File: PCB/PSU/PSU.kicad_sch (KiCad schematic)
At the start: 85 parts, among them J1 Backllight_Connector, J2 PSU_Jack, J3 PSU_Connector_Receptor, Q18 Q, Q22 8C, Q26 G16, Q27 8C, Q29 H15, Q32 K, Q34 6LS, Q5 8C, U12 J412, U13 J421, U5 K2337, U6 7064, U7 5W01, U8 FDS2734, U9 FDS2734

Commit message: Add files via upload
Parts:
- added C1, C16, C28, C46, C5, C59, C7: 150nF, symbol PCM_Elektuur:C
- added C10: 3.6nF, symbol PCM_Elektuur:C
- added C11, C15, C37: 180nF, symbol PCM_Elektuur:C
- added C12: 1.2uF, symbol PCM_Elektuur:C
- added C13, C14, C23, C41, C58: 1.5uF, symbol PCM_Elektuur:C
- added C17, C30, C32, C39, C9: 10nF, symbol PCM_Elektuur:C
- added C2: 4.7uF, symbol PCM_Elektuur:C
- added C21: 12nF, symbol PCM_Elektuur:C
- added C3: 5.2uF, symbol PCM_Elektuur:C
- added C35, C66: 1.2nF, symbol PCM_Elektuur:C
- added C4: 2.5nF, symbol PCM_Elektuur:C
- added C42, C51, C53, C64: 120nF, symbol PCM_Elektuur:C
- added C56, C61: 47uF, symbol PCM_Elektuur:C
- added C57: 15uF, symbol PCM_Elektuur:C
- added C6: 100pF, symbol PCM_Elektuur:C
- added C60: 1nF, symbol PCM_Elektuur:C
- added C62, C65: 100nF, symbol PCM_Elektuur:C
- added C63: 5.1nF, symbol PCM_Elektuur:C
- added C67: 18uF, symbol PCM_Elektuur:C
- added C8: 24nF, symbol PCM_Elektuur:C
- added D2: 5-9, symbol PCM_Elektuur:D
- added D3, R66, R95, R97: DNP, symbol PCM_Elektuur:C
- added D4: 18, symbol Device:D
- added D5: 3^9, symbol Device:D
- added D6, R1, R50, R82, R91: DNP, symbol PCM_Elektuur:R
- added F3: 15, symbol Device:Fuse
- added F4: 10, symbol Device:Fuse
- added L3: 68uH, symbol PCM_Elektuur:L
- added L4: 470uH, symbol PCM_Elektuur:L
- added Q1: R4C, symbol Device:D_Zener_Dual_CommonCathode_AAK_Split
- added Q10: 103 5G, symbol PSU:103_5G
- added Q11, Q14, Q24, Q3, Q6, Q7: 6LS, symbol Simulation_SPICE:PNP
- added Q12: Q, symbol Device:D_Schottky_Dual_CommonCathode_AAK_Split
- added Q13, Q15, Q33, Q37, Q4: 8LR, symbol Simulation_SPICE:NPN
- added Q16, Q17, Q19: M2P, symbol Device:D_Zener_Dual_CommonAnode_KAK
- added Q2: K, symbol Device:D_Dual_Series_KAC_Parallel
- added Q20, Q28, Q31: W6, symbol Device:D_Dual_CommonCathode_AKA
- added Q21, Q23, Q30, Q35: 8C, symbol Simulation_SPICE:NPN
- added Q25: 8LB, symbol Simulation_SPICE:NPN
- added Q36: 3P4J, symbol PCM_Elektuur:Th
- added Q8: 303 5H, symbol PSU:103_5G
- added Q9: KD 3.E, Package_TO_SOT_SMD:SOT-89-3, symbol Regulator_Linear:L78L05_SOT89
- added R10, R2, R21, R31, R74, R90: 470k, symbol PCM_Elektuur:R
- added R103, R11, R117, R13, R17, R19, R20, R30, R33, R35, R4, R61, R85: 10k, symbol PCM_Elektuur:R
- added R106, R27, R39, R41, R58, R60: 4.7k, symbol PCM_Elektuur:R
- added R107: 2k, symbol PCM_Elektuur:R
- added R109, R81: 200k, symbol PCM_Elektuur:R
- added R111: 33, symbol PCM_Elektuur:R
- added R112, R113, R18, R9: 20k, symbol PCM_Elektuur:R
- added R114, R15, R22, R54, R59, R72, R77, R84, R92: 100k, symbol PCM_Elektuur:R
- added R115: 11k, symbol PCM_Elektuur:R
- added R116: 15k, symbol PCM_Elektuur:R
- added R118, R48: 100, symbol PCM_Elektuur:R
- added R12: 2.2k, symbol PCM_Elektuur:R
- added R14: 12k, symbol PCM_Elektuur:R
- added R16: 130k, symbol PCM_Elektuur:R
- added R23, R25, R34: 0.1, symbol PCM_Elektuur:R
- added R24: 220, symbol PCM_Elektuur:R
- added R26: 103 (RT1), symbol PCM_Elektuur:R
- added R28: 0, symbol PCM_Elektuur:R
- added R29: 103 (RT2), symbol PCM_Elektuur:R
- added R3, R36, R65, R71, R75, R76, R93: 1k, symbol PCM_Elektuur:R
- added R37: 120, symbol PCM_Elektuur:R
- added R38, R6: 470, symbol PCM_Elektuur:R
- added R42, R47, R51, R70, R73, R79, R87, R94: 47k, symbol PCM_Elektuur:R
- added R53, R78: 300k, symbol PCM_Elektuur:R
- added R68: 74k, symbol PCM_Elektuur:R
- added R88, R89: 1M, symbol PCM_Elektuur:R
- added R96: 1.8k, symbol PCM_Elektuur:R
- added SW1: PSU-SW1, symbol Switch:SW_Push
- added U1: D9D, Package_TO_SOT_SMD:SOT-23-5, symbol Power_Management:BD48ExxG
- added U10: ~, symbol PSU:9742
- added U11, UU11: 7W14, symbol 74xGxx:74LVC3G14
- added U2: ~, symbol PSU:TA
- added U3: ~, symbol PSU:6.5_5F
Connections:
- net D18_2_3_PC110: now also J1.1 (Pin_1)
- net D28_1_PC110: now also C11.1 (+), C57.1 (+), C6.2 (-), Q10.4, R16.2 (-)
- net D2_3_PC110: now also Q23.1 (C)
- net F65_ENAVEE_PC110: now also R15.1 (+)
- net GND: now also R69.2 (-), C1.1 (+), C11.2 (-), C12.1 (+), C13.2 (-), C14.2 (-), C15.2 (-), C16.2 (-), C17.1 (+), C23.1 (+), C28.1 (+), C3.1 (+), C30.1 (+), C37.1 (+), C39.2 (-), C41.1 (+), C42.2 (-), C46.2 (-), C51.1 (+), C56.2 (-), C57.2 (-), C58.2 (-), C59.2 (-), C60.1 (+), C61.2 (-), C62.2 (-), C64.2 (-), C65.2 (-), C67.1 (+), C8.2 (-), C9.1 (+), D3.1 (+), D6.1 (+), Q10.2 (GND), Q12.1 (A), Q13.3 (E), Q19.2 (A), Q21.3 (E), Q23.3 (E), Q25.3 (E), Q33.3 (E), Q35.3 (E), Q36.1 (K-), Q37.3 (E), Q4.3 (E), Q8.2 (GND), Q9.2 (GND), R106.2 (-), R113.2 (-), R114.2 (-), R115.2 (-), R116.2 (-), R18.2 (-), R27.2 (-), R33.2 (-), R35.2 (-), R39.2 (-), R53.1 (+), R58.1 (+), R60.2 (-), R72.1 (+), R77.2 (-), R88.1 (+), R9.1 (+), R91.1 (+), R94.2 (-), R95.2 (-), R96.2 (-), U1.3 (GND), U10.8 (GND), U11.4 (GND), U2.2 (GND), U3.3 (GND); no longer R69.1 (+)
- net J5_33_PC110: now also C39.1 (+), R92.1 (+), R93.2 (-)
- net JRC_VCC: now also Q3.3 (E), R3.1 (+)
- net M38_P20_PC110: now also Q28.1 (A), Q37.2 (B)
- net M38_P21_PC110: now also Q28.3 (A)
- net M38_P52_PC110: now also R2.1 (+)
- net M38_P53_PC110: now also Q31.1 (A)
- net M38_P61_PC110: now also R42.1 (+)
- net M38_P64_PC110: now also U6.7, R54.2 (-), R66.2 (-)
- net M38_VREF_PC110: now also C1.2 (-), Q1.3 (K), Q14.3 (E), R6.1 (+)
- net PNET4_PC110: now also C53.2 (-), D2.2 (A+), Q11.3 (E), R22.2 (-)
- net PNET5_PC110: now also C28.2 (-), C56.1 (+), C61.1 (+), C62.1 (+), Q15.1 (C), Q2.3 (common), R118.1 (+), R17.2 (-), R20.2 (-), R23.1 (+), R25.1 (+), R26.1 (+), R29.2 (-), R34.1 (+), R84.2 (-), U11.8 (VCC), U2.5 (VCC)
- net PWR_IN_10v5: now also Q32.2 (A), C30.2 (-), D4.2 (A), Q24.3 (E), Q36.2 (A+), R75.2 (-), R95.1 (+)
- net Q49_1_PC110: now also D5.2 (A), R82.2 (-)
- net R284_2_PC110: now also C13.1 (+), C14.1 (+), F3.2, F4.2
- net R412_1_PC110: now also J1.2 (Pin_2)
- net R73_2_PC110: now also R79.2 (-)
- net U21_131_PC110: now also R10.2 (-)
- net U54_1D_PC110: now also R36.2 (-); no longer C31.1 (+), Q26.2 (G)
- net U54_VCC_PC110: now also C3.2 (-), Q3.2 (B), Q9.1 (OUT), SW1.2
- net at F5.2, L1.1 (+), Q34.3 (E): now also C37.2 (-), R89.2 (-), R91.2 (-)
- net at R52.1 (+), U6.12 (+): now also R69.1 (+), Q19.1 (K); no longer R69.2 (-)
- net at C27.1 (+), R55.1 (+), U7.1: now also Q16.1 (K)
- net at C29.1 (+), J2.2, R98.1 (+): now also R97.2 (-)
- net at C29.2 (-), F1.1, R99.1 (+): now also R97.1 (+)
- net at Q22.1 (C): now also Q35.1 (C), R73.2 (-)
- net at Q22.2 (B), Q5.2 (B), R5.2 (-): now also Q4.2 (B)
- net at U13.4 (G): now also U3.1, U3.4
- net at L1.2 (-), U13.5 (D), U13.6 (D)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: now also D6.2 (-)
- net at L5.1 (+), U4.15 (CS5): now also R23.2 (-), R25.2 (-), R34.2 (-)
- net at C18.1 (+), L5.2 (-), U4.17 (LX5)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: now also Q12.3 (K)
- net at JX.2 (Pin_2), R49.1 (+), R63.2 (-)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: now also Q19.3 (K)
- net at U7.3 (+): now also C46.1 (+), R103.1 (+), R109.1 (+), R113.1 (+)
- net at Q32.3 (common): now also R41.1 (+), R61.2 (-), U3.6
- net at C18.2 (-), U4.18 (BST5): now also Q17.1 (K)
- net at R5.1 (+): now also Q3.1 (C)
- net at C55.2 (-), U4.22 (VL): now also Q17.2 (A), R48.1 (+)
- net at U7.5 (+): now also R106.1 (+), R107.1 (+), R112.1 (+)
- net at U7.6 (-): now also C21.1 (+), R42.2 (-)
- net at U7.7: now also C21.2 (-), Q16.3 (K)
- net at Q34.2 (B): now also R90.1 (+)
- net at U6.5 (+): now also R77.1 (+), R78.1 (+)
- net at U6.6 (-): now also R53.2 (-), R54.1 (+), R66.1 (+)
- net at U4.12 (SHDN#), U4.13 (ON5), U4.3 (ON3)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: now also C23.2 (-), R48.2 (-)
- net at C19.2 (-), U4.25 (BST3): now also Q17.3 (K)
- new net: R93.1 (+), R94.1 (+), SW1.1
- new net: Q24.1 (C), R74.1 (+)
- new net: Q24.2 (B), R78.2 (-)
- new net: C31.1 (+), Q26.2 (G), R36.1 (+)
- new net: C41.2 (-), U10.15 (SCP)
- new net: C63.1 (+), C66.1 (+), U10.5 (FB1)
- new net: C63.2 (-), R117.1 (+), R13.2 (-), R33.1 (+), U10.4 (INV1)
- new net: R71.1 (+), R75.1 (+)
- new net: Q20.3 (A), R27.1 (+), R29.1 (+)
- new net: C17.2 (-), C32.2 (-), C67.2 (-), Q8.4, R81.2 (-)
- new net: C9.2 (-), Q7.1 (C), R15.2 (-), U10.7 (OUT1)
- new net: C8.1 (+), Q6.1 (C), R10.1 (+)
- new net: C60.2 (-), R65.1 (+), U10.1 (CT)
- new net: R50.2 (-), R65.2 (-), U2.3
- new net: C32.1 (+), Q7.3 (E), R115.1 (+), R79.1 (+), R81.1 (+), U10.3 (NON1)
- new net: C6.1 (+), Q6.3 (E), R116.1 (+), R16.1 (+), U10.14 (NON2)
- new net: Q16.2 (A), R51.1 (+), R60.1 (+)
- new net: Q21.1 (C), R59.1 (+)
- new net: Q28.2 (K), Q31.3 (A), R47.2 (-), R59.2 (-)
- new net: R28.1 (+), R31.2 (-), U1.1 (VOUT)
- new net: R21.2 (-), R28.2 (-)
- new net: C2.1 (+), R4.1 (+)
- new net: R1.2 (-), R11.1 (+), R35.1 (+), R4.2 (-), U10.13 (INV2)
- new net: D4.1 (K), R76.1 (+)
- new net: C42.1 (+), Q36.3 (G), R76.2 (-), R96.1 (+)
- new net: C5.2 (-), R18.1 (+), R19.1 (+), U10.11 (DT2)
- new net: C5.1 (+), C58.1 (+), C59.1 (+), C7.2 (-), Q6.2 (B), Q7.2 (B), R11.2 (-), R13.1 (+), R14.1 (+), R19.2 (-), U10.16 (VREF)
- new net: Q21.2 (B), R68.2 (-)
- new net: Q30.3 (E), R50.1 (+), U2.4
- new net: C4.1 (+), R24.2 (-)
- new net: C4.2 (-), R12.2 (-), U11.2
- new net: Q20.1 (A), R26.2 (-), R58.2 (-)
- new net: Q14.2 (B), R68.1 (+)
- new net: L4.1 (+), Q8.3, Q8.5
- new net: C65.1 (+), F4.1, L4.2 (-)
- new net: C7.1 (+), R14.2 (-), R9.2 (-), U10.6 (DT1)
- new net: Q10.1, R37.1 (+), R38.1 (+)
- new net: C10.1 (+), R38.2 (-), U11.5, UU11.7
- new net: Q23.2 (B), R71.2 (-), R72.2 (-), R73.1 (+)
- new net: R88.2 (-), R89.1 (+)
- new net: Q2.1 (K), R3.2 (-)
- new net: Q4.1 (C), R2.2 (-)
- new net: Q1.1 (A), Q14.1 (C), R103.2 (-), R109.2 (-), R112.2 (-)
- new net: R20.1 (+), U11.6
- new net: Q13.1 (C), R30.1 (+)
- new net: D2.1 (K-), Q11.2 (B), R30.2 (-)
- new net: C16.1 (+), R21.1 (+), R22.1 (+), U1.2 (VDD)
- new net: Q15.2 (B), R47.1 (+)
- new net: Q15.3 (E), R51.2 (-)
- new net: R17.1 (+), U10.10 (OUT2), U11.3, UU11.1
- new net: Q31.2 (K), R70.1 (+), R87.2 (-)
- new net: Q25.2 (B), R70.2 (-)
- new net: Q33.1 (C), R90.2 (-)
- new net: Q33.2 (B), R87.1 (+)
- new net: D5.1 (K), Q20.2 (K), R82.1 (+)
- new net: C64.1 (+), R118.2 (-), U10.9 (VCC)
- new net: C2.2 (-), R1.1 (+), U10.12 (FB2)
- new net: Q13.2 (B), R31.1 (+)
- new net: C12.2 (-), D3.2 (-), Q11.1 (C), Q9.3 (IN)
- new net: Q25.1 (C), R74.2 (-)
- new net: Q2.2 (A), R6.2 (-)
- new net: C66.2 (-), R117.2 (-)
- new net: C35.2 (-), Q30.1 (C), R85.2 (-)
- new net: Q30.2 (B), R84.1 (+)
- new net: Q35.2 (B), R92.2 (-)
- new net: C15.1 (+), F3.1, L3.1 (+)
- new net: C51.2 (-), R111.1 (+)
- new net: C53.1 (+), R111.2 (-)
- new net: C10.2 (-), R37.2 (-)
- new net: L3.2 (-), Q10.3, Q10.5
- new net: Q37.1 (C), R107.2 (-)
- new net: C35.1 (+), R61.1 (+), R85.1 (+), U3.2, U3.5
- new net: Q8.1, R12.1 (+), R24.1 (+)
- new net: R39.1 (+), R41.2 (-)
- new net: R114.1 (+), U10.2 (RT)
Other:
- moved on the sheet: C18, C19, C20, C22, C24, C25, C26, C27, C29, C31, C33, C34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

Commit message: Add files via upload
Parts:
- added unit 2 of Q1
- added unit 2 of Q12
- renumbered JX to JX1, UU11 to U11
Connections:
- net GND: now also Q12.2 (A)
- net M38_VREF_PC110: now also Q1.3 (K)
- net Q43_2_PC110: now also C17.2 (-), C32.2 (-), C67.2 (-), Q8.4, R81.2 (-)
- net at Q16.2 (A), R51.1 (+), R60.1 (+): now also U2.1
- net at C18.1 (+), L5.2 (-), Q12.3 (K)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: now also Q12.3 (K)
- no-connect marks 2 -> 3

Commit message: Add files via upload
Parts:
- removed D1: 8-2, symbol Device:D
- removed Q11, Q14, Q24: 6LS, symbol Simulation_SPICE:PNP
- removed Q12: Q, symbol Device:D_Schottky_Dual_CommonCathode_AAK_Split
- removed Q13, Q15, Q33, Q37: 8LR, symbol Simulation_SPICE:NPN
- removed Q22, Q23, Q27, Q30, Q35, Q5: 8C, symbol Simulation_SPICE:NPN
- removed Q25: 8LB, symbol Simulation_SPICE:NPN
- removed Q26: G16, Package_TO_SOT_THT:TO-92_Inline, symbol Transistor_FET:2N7000
- removed Q29: H15, Package_TO_SOT_THT:TO-92L_Inline, symbol Transistor_FET:TP0610L
- removed Q32: K, symbol Device:D_Dual_Series_KAC_Parallel
- added D1: 8-2, symbol Device:D_Zener
- added Q11, Q14: 6LS, symbol PCM_Transistor_BJT_AKL:Q_PNP_Generic_BEC
- added Q12: Q, symbol Device:D_Zener_Dual_CommonAnode_KAK
- added Q13, Q15, Q25, Q33, Q37: 8LR, symbol PCM_Transistor_BJT_AKL:Q_NPN_Generic_BEC
- added Q22, Q5: 8C, symbol PCM_Transistor_BJT_AKL:Q_NPN_Generic_CEB
- added Q23, Q27, Q30, Q35: 8C, symbol PCM_Transistor_BJT_AKL:Q_NPN_Generic_BEC
- added Q24: 6LS, symbol PCM_Transistor_BJT_AKL:Q_PNP_Generic_CEB
- added Q26: G16, PCM_Package_TO_SOT_SMD_AKL:SOT-23, symbol PCM_Transistor_MOSFET_AKL:2N7002AQ
- added Q29: H15, Package_TO_SOT_SMD:SOT-23, symbol Transistor_FET:AO3401A
- added Q32: K, symbol Device:D_Dual_Series_ACK_Parallel
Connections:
- net D2_3_PC110: now also Q23.3 (C)
- net GND: now also C34.2 (-), C56.1 (+), C58.1 (+), C62.1 (+), Q1.1 (A), R105.2 (-), R116.1 (+), R27.1 (+), Q12.1 (K), Q12.3 (K), Q13.2 (E), Q22.2 (E), Q23.2 (E), Q25.2 (E), Q26.2 (S), Q27.2 (E), Q33.2 (E), Q35.2 (E), Q37.2 (E), Q5.2 (E); no longer C34.1 (+), C56.2 (-), C58.2 (-), C62.2 (-), R105.1 (+), R116.2 (-), R27.2 (-)
- net J5_6_PC110: now also D1.1 (K), Q32.1 (A)
- net M38_P20_PC110: now also Q37.1 (B)
- net M38_P60_PC110: now also C25.1 (+), R62.1 (+); no longer C25.2 (-), R62.2 (-)
- net M38_P61_PC110: now also C52.1 (+), R101.1 (+); no longer C52.2 (-), R101.2 (-)
- net M38_P64_PC110: now also R54.1 (+), R66.1 (+); no longer R54.2 (-), R66.2 (-)
- net M38_VREF_PC110: now also Q14.2 (E)
- net PNET4_PC110: now also D2.1 (K-), Q11.2 (E), Q29.2 (S); no longer D2.2 (A+)
- net PNET5_PC110: now also C56.2 (-), C62.2 (-), Q15.3 (C); no longer C56.1 (+), C62.1 (+)
- net PWR_IN_10v5: now also D4.1 (K), Q24.2 (E), Q32.3 (K); no longer D4.2 (A)
- net U54_VCC_PC110: now also SW1.1; no longer SW1.2
- net at R93.1 (+), R94.1 (+): now also SW1.2; no longer SW1.1
- net at R74.1 (+): now also Q24.1 (C)
- net at R78.2 (-): now also Q24.3 (B)
- net at F5.1, JX1.1 (Pin_1): no longer R52.2 (-)
- net at C31.1 (+), R36.1 (+): now also Q26.1 (G)
- net at C27.1 (+), R55.1 (+): now also R67.1 (+), U7.2 (-); no longer Q16.1 (K), U7.1
- net at C27.2 (-), R55.2 (-): now also Q16.1 (K), U7.1; no longer R67.1 (+), U7.2 (-)
- net at Q20.3 (A), R29.1 (+): now also R27.2 (-); no longer R27.1 (+)
- net at R46.1 (+): now also Q26.3 (D), Q29.1 (G)
- net at R73.2 (-): now also Q22.1 (C), Q35.3 (C)
- net at Q4.2 (B), R5.2 (-): now also Q22.3 (B), Q5.3 (B)
- net at C6.1 (+), Q6.3 (E), R16.1 (+)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: now also R116.2 (-); no longer R116.1 (+)
- net at JX1.2 (Pin_2), R49.1 (+), R63.2 (-)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: now also R52.2 (-); no longer Q19.3 (K)
- net at C18.1 (+), L5.2 (-), U4.17 (LX5)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: now also Q12.2 (A)
- net at R63.1 (+), U6.9 (-): now also C25.2 (-), Q19.3 (K), R62.2 (-); no longer C25.1 (+), R62.1 (+)
- net at R76.1 (+): now also D4.2 (A); no longer D4.1 (K)
- net at C5.1 (+), C59.1 (+), C7.2 (-)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: now also C58.2 (-); no longer C58.1 (+)
- net at R50.1 (+), U2.4: now also Q30.2 (E)
- net at R64.2 (-), U6.13 (-): now also C52.2 (-), R101.2 (-); no longer C52.1 (+), R101.1 (+)
- net at R68.1 (+): now also Q14.1 (B)
- net at R41.1 (+), R61.2 (-), U3.6: now also Q32.2 (common)
- net at R53.2 (-), U6.6 (-): now also R54.2 (-), R66.2 (-); no longer R54.1 (+), R66.1 (+)
- net at R71.2 (-), R72.2 (-), R73.1 (+): now also Q23.1 (B)
- net at C36.2 (-), R83.2 (-), R86.1 (+)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: now also Q29.3 (D)
- net at C33.2 (-): now also C34.1 (+), R80.1 (+), Q27.1 (B); no longer R86.2 (-)
- net at R103.2 (-), R109.2 (-), R112.2 (-): now also Q14.3 (C); no longer Q1.1 (A)
- net at R30.1 (+): now also Q13.3 (C)
- net at R30.2 (-): now also D2.2 (A+), Q11.1 (B); no longer D2.1 (K-)
- net at R47.1 (+): now also Q15.1 (B)
- net at R51.2 (-): now also Q15.2 (E)
- net at R70.2 (-): now also Q25.1 (B)
- net at R90.2 (-): now also Q33.3 (C)
- net at R87.1 (+): now also Q33.1 (B)
- net at C43.1 (+), R102.1 (+), U6.3 (+): now also R105.1 (+); no longer R105.2 (-)
- net at R31.1 (+): now also Q13.1 (B)
- net at C12.2 (-), D3.2 (-), Q9.3 (IN): now also Q11.3 (C)
- net at R74.2 (-): now also Q25.3 (C)
- net at R85.2 (-): now also C35.1 (+), R61.1 (+), U3.2, U3.5; no longer C35.2 (-)
- net at R84.1 (+): now also Q30.1 (B)
- net at R92.2 (-): now also Q35.1 (B)
- net at R107.2 (-): now also Q37.3 (C)
- new net: C33.1 (+), Q27.3 (C), R86.2 (-)
- new net: D1.2 (A), Q5.1 (C)
- new net: C35.2 (-), Q30.3 (C), R85.1 (+)
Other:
- moved on the sheet: C1, C25, C27, C33, C34, C52, C58, C62, Q1A, R101, R105, R116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

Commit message: Add files via upload
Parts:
- removed Q4: 8LR, symbol Simulation_SPICE:NPN
- added Q4: 8LR, symbol PCM_Transistor_BJT_AKL:Q_NPN_Generic_CEB
- C1, C10, C11, C15, C16, C17, C18, C19, C21, C22, C24, C25, C26, C27, C28, C29, C30, C31, C32, C33, C35, C36, C37, C39, C4, C40, C42, C43, C44, C46, C47, C48, C49, C5, C51, C52, C53, C59, C6, C60, C62, C63, C64, C65, C66, C7, C8, C9: footprint (none) -> Capacitor_SMD:C_0603_1608Metric; Indicator + -> (none); Rating V -> (none)
- C12, C13, C14, C3: footprint (none) -> Capacitor_SMD:C_1206_3216Metric; Indicator + -> (none); Rating V -> (none)
- C2: value 4.7uF -> 4.7nF; footprint (none) -> Capacitor_SMD:C_0603_1608Metric; Indicator + -> (none); Rating V -> (none)
- C20: value 1.2nF -> 100pF; footprint (none) -> Capacitor_SMD:C_0603_1608Metric; Indicator + -> (none); Rating V -> (none)
- C23, C34, C38, C41, C55, C58: footprint (none) -> Capacitor_SMD:C_0805_2012Metric; Indicator + -> (none); Rating V -> (none)
- C45: value 33uF -> 33uF 20V; footprint (none) -> Capacitor_THT:C_Disc_D3.0mm_W1.6mm_P2.50mm; Indicator + -> (none); Rating V -> (none)
- C50: value 56uF -> 56uF 25V EC; footprint (none) -> Capacitor_THT:EC; Indicator + -> (none); Rating V -> (none)
- C54, C61: value 47uF -> 47uF 6.3v; footprint (none) -> Capacitor_THT:C_Radial_D6.3mm_H11.0mm_P2.50mm; Indicator + -> (none); Rating V -> (none)
- C56: value 47uF -> 47uF 6.3V; footprint (none) -> Capacitor_THT:C_Radial_D6.3mm_H11.0mm_P2.50mm; Indicator + -> (none); Rating V -> (none)
- C57: value 15uF -> 15uF 16V; footprint (none) -> Capacitor_THT:C_Radial_D6.3mm_H11.0mm_P2.50mm; Indicator + -> (none); Rating V -> (none)
- C67: value 18uF -> 18uF 50V; footprint (none) -> Capacitor_THT:C_Radial_D6.3mm_H11.0mm_P2.50mm; Indicator + -> (none); Rating V -> (none)
- D1, D4, D5: footprint (none) -> Diode_SMD:D_0603_1608Metric
- D2: footprint (none) -> Diode_SMD:D_0603_1608Metric; Rating V/A -> (none)
- D3: footprint (none) -> Diode_SMD:D_1206_3216Metric; Indicator + -> (none); Rating V -> (none); now not fitted
- D6: footprint (none) -> Diode_SMD:D_1206_3216Metric; Indicator + -> (none); Rating W -> (none); now not fitted
- D7, D8: footprint (none) -> Diode_SMD:D_1206_3216Metric; Rating V/A -> (none)
- F1, F2, F5: footprint (none) -> Fuse:Fuse_2010_5025Metric
- F3: footprint (none) -> Fuse:Fuse_1206_3216Metric
- F4: footprint (none) -> Fuse:Fuse_1210_3225Metric
- J1: footprint (none) -> Connector_JST:Backllight_Connector
- J2: footprint (none) -> PSU:PSU_Jack
- J3: footprint (none) -> PSU:PSU_Connector_Receptor
- L1: footprint (none) -> Inductor_THT:L_Radial_D7.5mm_P5.00mm_Fastron_07P; Indicator ● -> (none); Rating A -> (none)
- L2, L5: footprint (none) -> Inductor_THT:L_Radial_D10.0mm_P5.00mm_Fastron_07M; Indicator ● -> (none); Rating A -> (none)
- L3, L4: footprint (none) -> Inductor_SMD:L_Coilcraft_LPS5030; Indicator ● -> (none); Rating A -> (none)
- Q1, Q12, Q16, Q17, Q18, Q19, Q2, Q20, Q28, Q31, Q32: footprint (none) -> PC110:3D
- Q10, Q8: footprint (none) -> Package_TO_SOT_SMD:SOT-powerT
- Q11, Q13, Q14, Q15, Q21, Q22, Q23, Q24, Q27, Q3, Q30, Q33, Q34, Q35, Q37, Q5, Q6, Q7: footprint (none) -> Package_TO_SOT_SMD:SOT-416
- Q25: value 8LR -> 8LB; footprint (none) -> Package_TO_SOT_SMD:SOT-416
- Q26: footprint PCM_Package_TO_SOT_SMD_AKL:SOT-23 -> Package_TO_SOT_SMD:SOT-23-PC110
- Q29: footprint Package_TO_SOT_SMD:SOT-23 -> Package_TO_SOT_SMD:SOT-23-PC110
- Q36: footprint (none) -> Package_TO_SOT_SMD:TO-252-2; Rating V/A -> (none)
- R1: footprint (none) -> Resistor_SMD:R_0603_1608Metric; Indicator + -> (none); Rating W -> (none); now not fitted
- R10, R100, R101, R102, R103, R104, R105, R106, R107, R108, R109, R11, R110, R111, R112, R113, R116, R117, R118, R12, R13, R14, R15, R16, R17, R18, R19, R2, R20, R21, R22, R24, R27, R28, R3, R30, R31, R33, R35, R36, R37, R38, R39, R4, R41, R42, R43, R44, R45, R46, R47, R48, R49, R5, R50, R52, R53, R54, R55, R56, R57, R58, R59, R6, R60, R61, R62, R63, R64, R65, R67, R69, R71, R73, R74, R75, R76, R77, R78, R79, R80, R81, R82, R83, R84, R85, R86, R88, R89, R9, R90, R92, R93, R94, R96: footprint (none) -> Resistor_SMD:R_0603_1608Metric; Indicator + -> (none); Rating W -> (none)
- R114: value 100k -> 10k; footprint (none) -> Resistor_SMD:R_0603_1608Metric; Indicator + -> (none); Rating W -> (none)
- R115: value 11k -> 11K; footprint (none) -> Resistor_SMD:R_0603_1608Metric; Indicator + -> (none); Rating W -> (none)
- R23, R25, R26, R29, R32, R34, R40, R91, R98, R99: footprint (none) -> Resistor_SMD:R_1206_3216Metric; Indicator + -> (none); Rating W -> (none)
- R51: value 47k -> 4.7k; footprint (none) -> Resistor_SMD:R_0603_1608Metric; Indicator + -> (none); Rating W -> (none)
- R66: footprint (none) -> Resistor_SMD:R_0603_1608Metric; Indicator + -> (none); Rating V -> (none); now not fitted
- R68: value 74k -> 47k; footprint (none) -> Resistor_SMD:R_0603_1608Metric; Indicator + -> (none); Rating W -> (none)
- R7, R8: footprint (none) -> Resistor_SMD:R_1210_3225Metric; Indicator + -> (none); Rating W -> (none)
- R70, R87: value 47k -> 470k; footprint (none) -> Resistor_SMD:R_0603_1608Metric; Indicator + -> (none); Rating W -> (none)
- R72: value 100k -> 1k; footprint (none) -> Resistor_SMD:R_0603_1608Metric; Indicator + -> (none); Rating W -> (none)
- R95, R97: footprint (none) -> Resistor_SMD:R_1206_3216Metric; Indicator + -> (none); Rating V -> (none); now not fitted
- SW1: footprint (none) -> PSU:PSU-SW1
- U10: value ~ -> 9742; footprint (none) -> Package_SO:SSOP-16_4.4x5.2mm_P0.65mm
- U11, U7: footprint (none) -> PSU:SSOP-8-PSU
- U12: value J412 -> J421; footprint Package_SO:SOIC-8_3.9x4.9mm_P1.27mm -> Package_SO:SOP-8_3.9x4.9mm_P1.27mm
- U13, U5: footprint Package_SO:SOIC-8_3.9x4.9mm_P1.27mm -> Package_SO:SOP-8_3.9x4.9mm_P1.27mm
- U2: value ~ -> TA; footprint (none) -> Package_TO_SOT_SMD:SOT-23-5
- U3: value ~ -> 6.5 5F; footprint (none) -> Package_TO_SOT_SMD:SOT-23-6_Handsoldering
- U4: value ~ -> MAX786CAI; footprint (none) -> Package_SO:TSSOP-28_6.1x9.7mm_P0.65mm
- U6: footprint (none) -> Package_SO:TSSOP-14_4.4x5mm_P0.65mm
- U8, U9: value FDS2734 -> 2556; footprint Package_SO:SOIC-8_3.9x4.9mm_P1.27mm -> Package_SO:SOP-8_3.9x4.9mm_P1.27mm
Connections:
- net GND: now also Q4.2 (E)
- net at R2.2 (-): now also Q4.1 (C)
- net at Q22.3 (B), Q5.3 (B), R5.2 (-): now also Q4.3 (B)
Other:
- moved on the sheet: C31

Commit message: Add files via upload
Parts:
- Q4: footprint (none) -> Package_TO_SOT_SMD:SOT-416
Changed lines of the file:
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@@
 			)
 		)
-		(property "Footprint" ""
+		(property "Footprint" "Package_TO_SOT_SMD:SOT-416"
 			(at 246.38 256.54 0)
 			(effects
@@
 			)
 		)
-		(property "Description" "NPN transistor, generic symbol, Alternate KiCAD Library"
+		(property "Description" ""
 			(at 251.46 259.08 0)
 			(effects

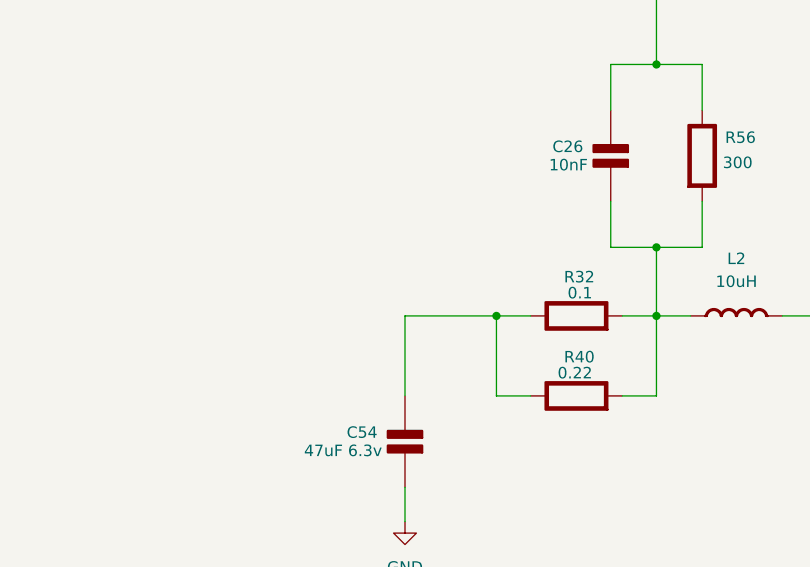
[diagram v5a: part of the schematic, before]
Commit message: fixed connection with 3V3 buck output and PNET1
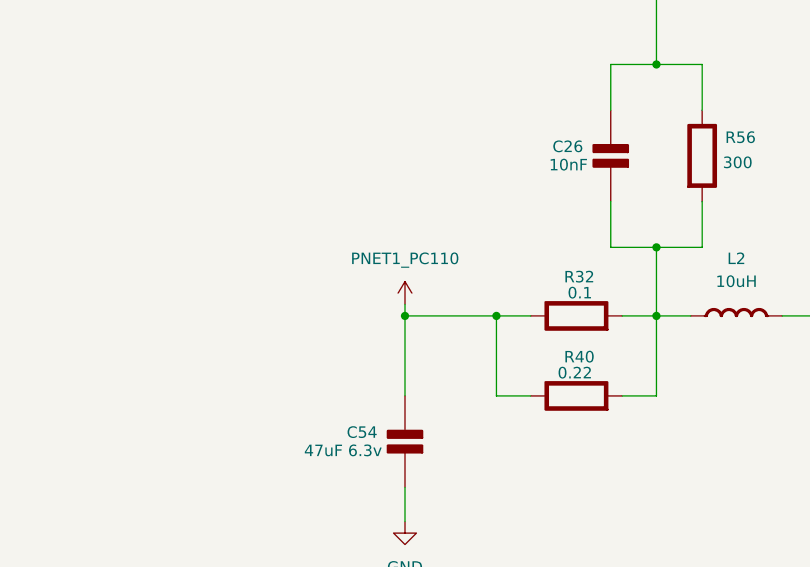
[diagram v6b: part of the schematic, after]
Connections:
- net PNET1_PC110: now also C54.2 (-), R32.1 (+), R40.1 (+)
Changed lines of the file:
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@@
 	)
 	(junction
+		(at 468.63 312.42)
+		(diameter 0)
+		(color 0 0 0 0)
+	)
+	(junction
 		(at 74.93 443.23)
 		(diameter 0)
@@
 	(wire
 		(pts
+			(xy 468.63 311.15) (xy 468.63 312.42)
+		)
+		(stroke
+			(width 0)
+			(type default)
+		)
+	)
+	(wire
+		(pts
 			(xy 657.86 149.86) (xy 657.86 152.4)
 		)
@@
 					(unit 1)
 				)
+			)
+		)
+	)
+	(symbol
+		(lib_id "power:VCC")
+		(at 468.63 311.15 0)
+		(unit 1)
+		(exclude_from_sim no)
+		(in_bom yes)
+		(on_board yes)
+		(dnp no)
+		(fields_autoplaced yes)
+		(property "Reference" "#PWR0128"
+			(at 468.63 314.96 0)
+			(effects
+				(font
+					(size 1.27 1.27)
+				)
+				(hide yes)
+			)
+		)
+		(property "Value" "PNET1_PC110"
+			(at 468.63 306.07 0)
+			(effects
+				(font
+					(size 1.27 1.27)
+				)
+			)
+		)
+		(property "Footprint" ""
+			(at 468.63 311.15 0)
+			(effects
+				(font
+					(size 1.27 1.27)
+				)
+				(hide yes)
+			)
+		)
+		(property "Datasheet" ""
+			(at 468.63 311.15 0)
+			(effects
+				(font
+					(size 1.27 1.27)
+				)
+				(hide yes)
+			)
+		)
+		(property "Description" "Power symbol creates a global label with name \"VCC\""
+			(at 468.63 311.15 0)
+			(effects
+				(font
+					(size 1.27 1.27)
+				)
+				(hide yes)
+			)
+		)
+		(pin "1"
+		)
+		(instances
+			(project "PSU"
+				(path "/af346fe7-2682-41ae-8d2a-5a211ef6d3f0"
+					(reference "#PWR0128")
+					(unit 1)
+				)
